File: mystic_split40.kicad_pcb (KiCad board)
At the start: 2 copper layers, 95.2 x 93.8 mm, 121 parts, among them J15 RESET, J16 ISP, J17 WS2812, J18 SJ-43514-SMT, J22 AREF, J25 TYPE-C-31-M-12, J33 RESET, J34 ISP, J35 WS2812, J36 SJ-43514-SMT, J4 AREF, J7 TYPE-C-31-M-12, SW1 EC11E, SW2 EC11E, U1 ATmega32U4-AU, U2 ATmega32U4-AU, Y1 CSTNE16M0VH3L000R0, Y2 CSTNE16M0VH3L000R0

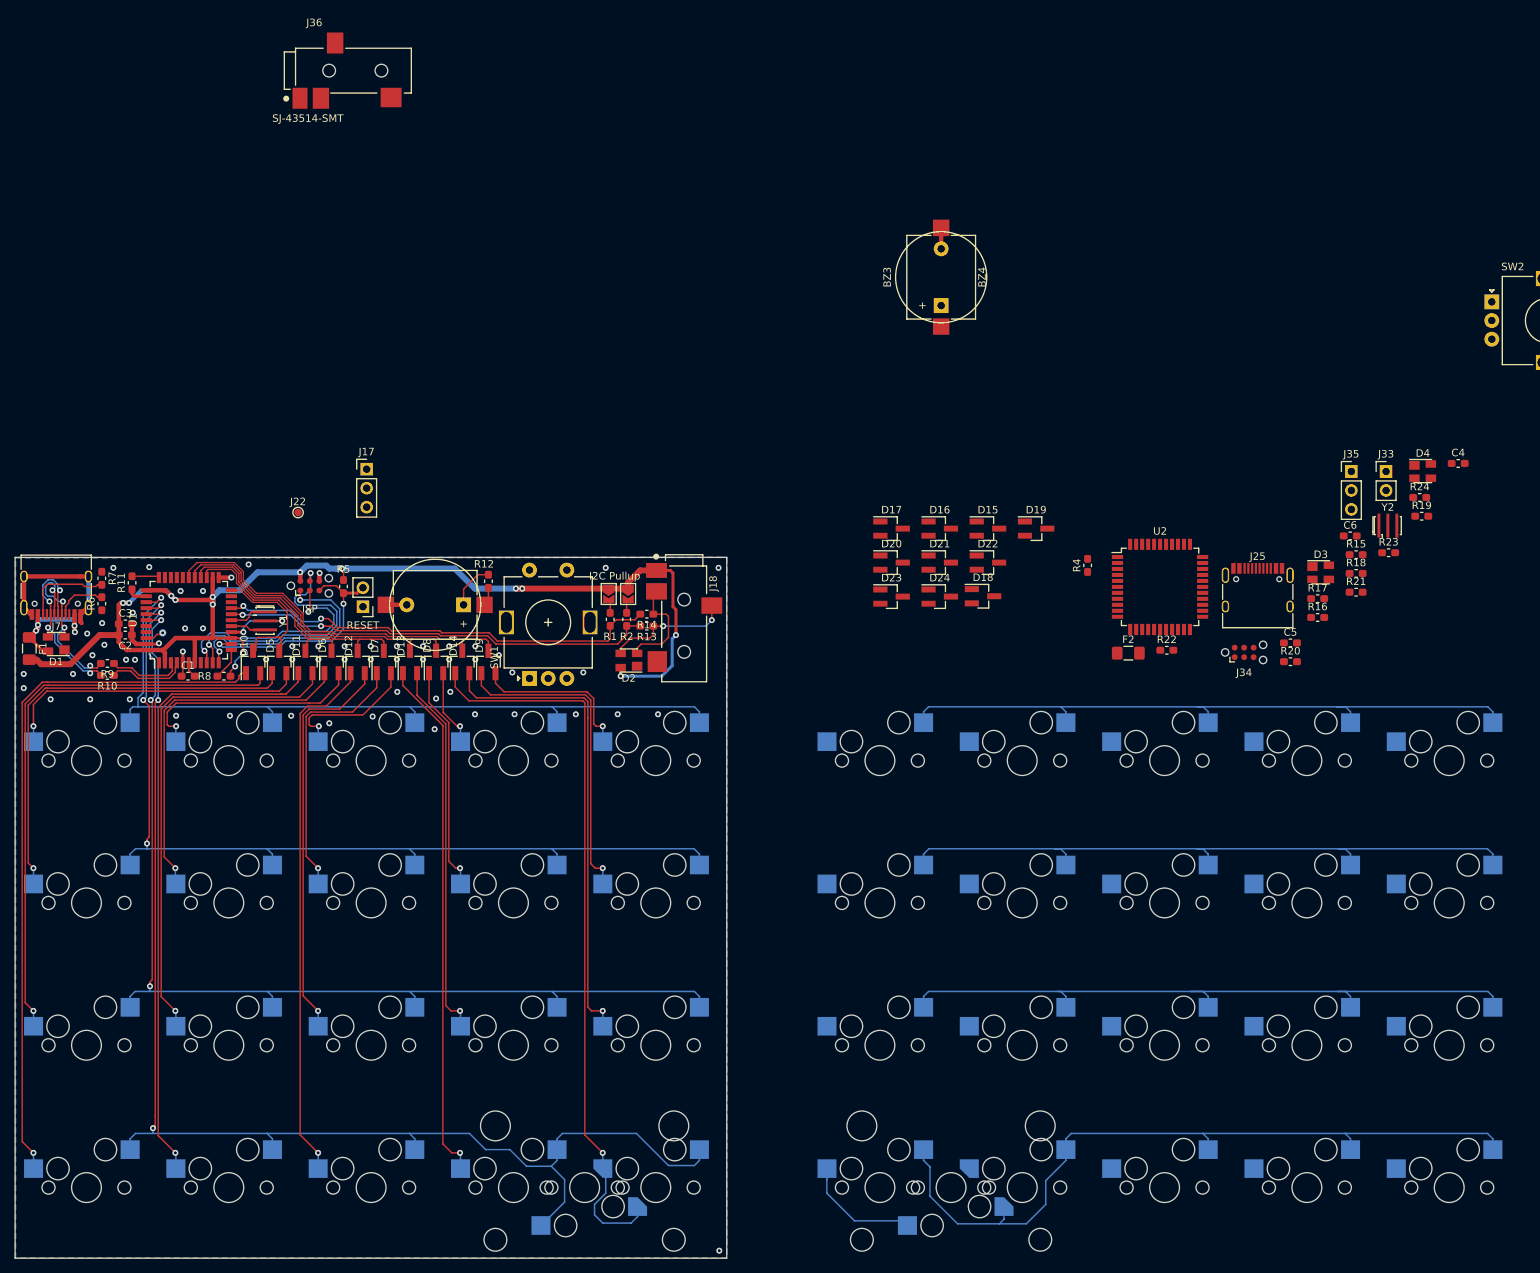
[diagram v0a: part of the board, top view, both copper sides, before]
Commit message: Added 3D models, prettied up silk
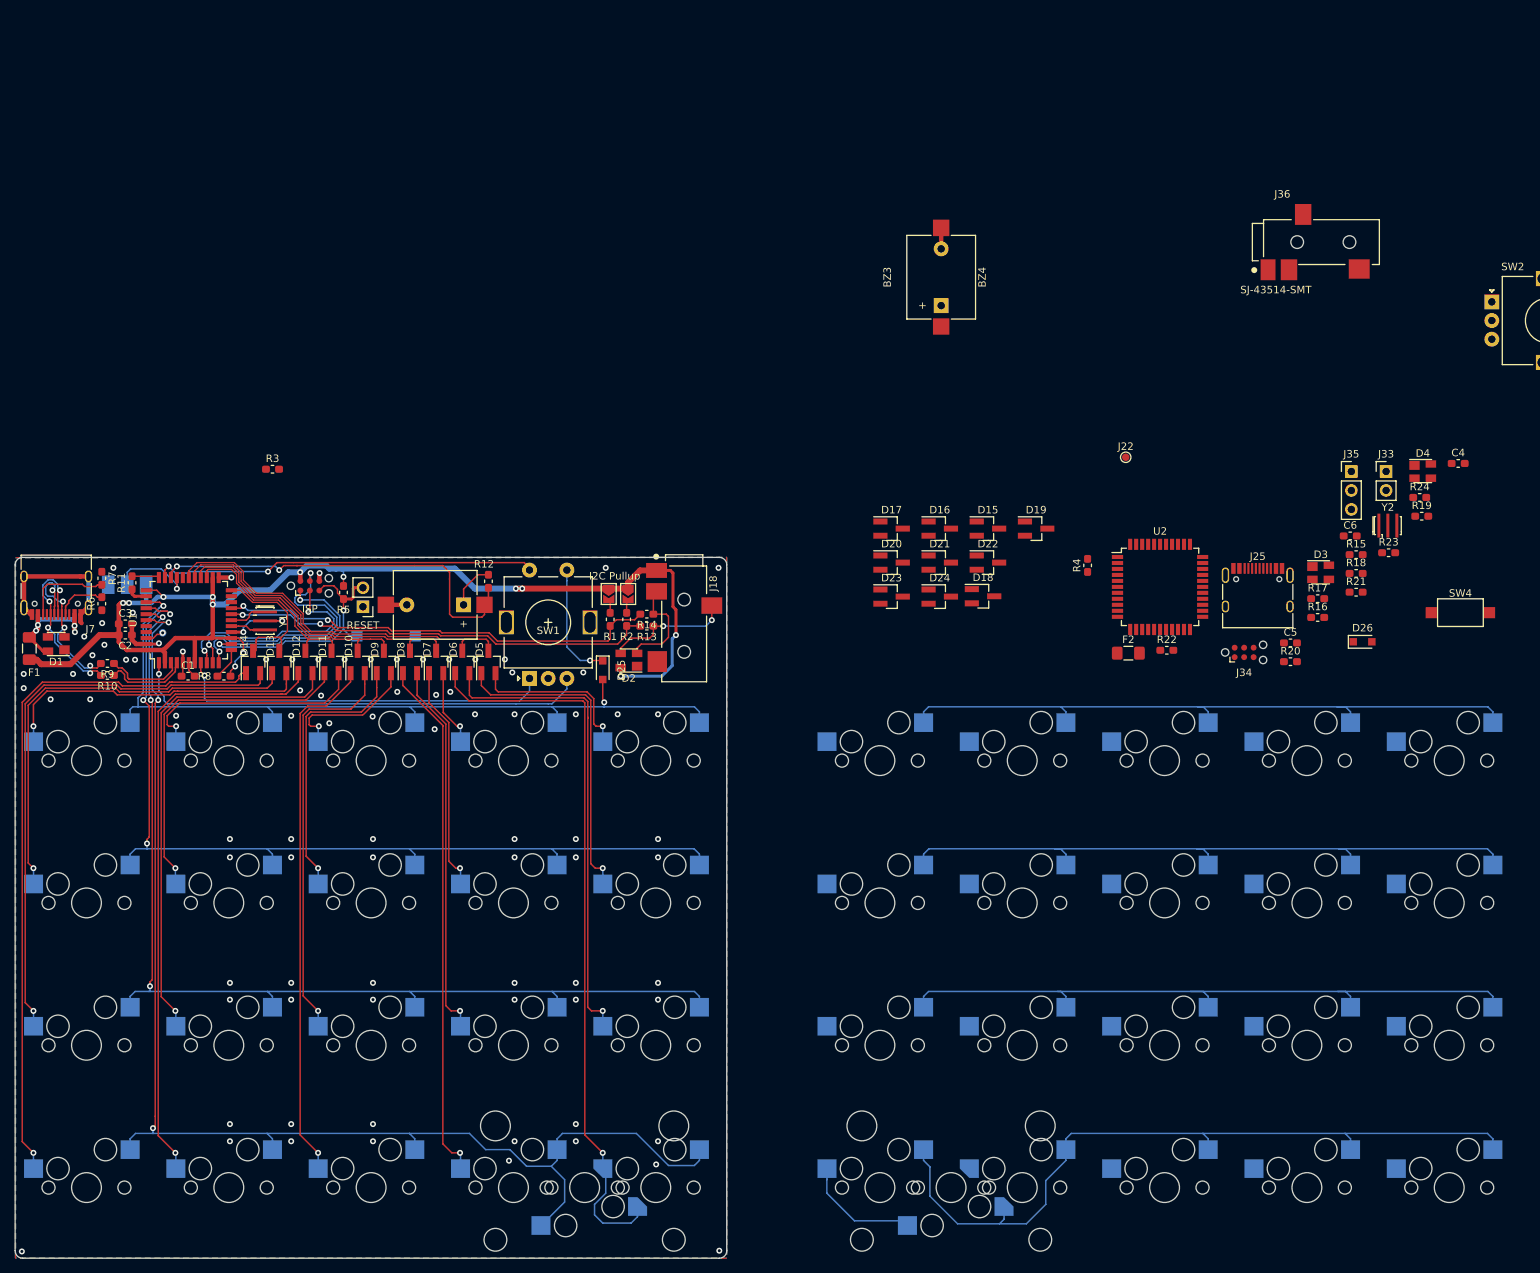
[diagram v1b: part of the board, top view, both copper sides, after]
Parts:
- added D25: BAV70, Diode_SMD:D_SOD-323_HandSoldering, F.Cu at (118.9, 27.8)
- added D26: BAV70, Diode_SMD:D_SOD-323_HandSoldering, F.Cu at (220.6, 24.0)
- added R3: 220R, Resistor_SMD:R_0603_1608Metric_Pad1.05x0.95mm_HandSolder, F.Cu at (74.7, 0.90)
- added SW3: Reset, Button_Switch_SMD:SW_SPST_CK_RS282G05A3, B.Cu at (89.9, 23.2)
- added SW4: Reset, Button_Switch_SMD:SW_SPST_CK_RS282G05A3, F.Cu at (233.7, 20.1)
- J17: moved to B.Cu
- R4: value 5k1 -> 220R
- moved J36 131.6 mm to (215.1, -29.5)
- moved J22 111.0 mm to (188.9, -0.70)
- moved J17 37.9 mm to (52.7, 16.4), turned to 270 degrees
- moved R5 0.80 mm to (84.2, 17.4)
- renumbered D12 to D10, D6 to D11, D11 to D12, D5 to D13, D10 to D14, D9 to D5, D14 to D6, D8 to D7, D13 to D8, D7 to D9
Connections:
- D15 pad 3: /Matrix right/col0 -> /Matrix right/col4
- D16 pad 3: /Matrix right/col1 -> /Matrix right/col4
- D17 pad 3: /Matrix right/col2 -> /Matrix right/col3
- D19 pad 3: /Matrix right/col4 -> /Matrix right/col2
- D20 pad 3: /Matrix right/col0 -> /Matrix right/col2
- D22 pad 3: /Matrix right/col2 -> /Matrix right/col1
- D23 pad 3: /Matrix right/col3 -> /Matrix right/col0
- D24 pad 3: /Matrix right/col4 -> /Matrix right/col0
- J25 pad A8: Net-(J25-PadA8) -> (no net)
- J25 pad B8: Net-(J25-PadB8) -> (no net)
- J7 pad A8: Net-(J7-PadA8) -> (no net)
- J7 pad B8: Net-(J7-PadB8) -> (no net)
- MX21 pad 1: Net-(D15-Pad2) -> Net-(D23-Pad2)
- MX22 pad 1: Net-(D16-Pad2) -> Net-(D21-Pad2)
- MX23 pad 1: Net-(D17-Pad2) -> Net-(D19-Pad2)
- MX24 pad 1: Net-(D18-Pad2) -> Net-(D17-Pad2)
- MX25 pad 1: Net-(D19-Pad2) -> Net-(D15-Pad2)
- MX26 pad 1: Net-(D15-Pad1) -> Net-(D23-Pad1)
- MX27 pad 1: Net-(D16-Pad1) -> Net-(D21-Pad1)
- MX28 pad 1: Net-(D17-Pad1) -> Net-(D19-Pad1)
- MX29 pad 1: Net-(D18-Pad1) -> Net-(D17-Pad1)
- MX30 pad 1: Net-(D19-Pad1) -> Net-(D15-Pad1)
- MX31 pad 1: Net-(D20-Pad2) -> Net-(D24-Pad2)
- MX32 pad 1: Net-(D21-Pad2) -> Net-(D22-Pad2)
- MX33 pad 1: Net-(D22-Pad2) -> Net-(D20-Pad2)
- MX34 pad 1: Net-(D23-Pad2) -> Net-(D18-Pad2)
- MX35 pad 1: Net-(D24-Pad2) -> Net-(D16-Pad2)
- MX36 pad 1: Net-(D20-Pad1) -> Net-(D24-Pad1)
- MX37 pad 1: Net-(D21-Pad1) -> Net-(D22-Pad1)
- MX38 pad 1: Net-(D22-Pad1) -> Net-(D20-Pad1)
- MX39 pad 1: Net-(D23-Pad1) -> Net-(D18-Pad1)
- MX40 pad 1: Net-(D24-Pad1) -> Net-(D16-Pad1)
- MX42 pad 1: Net-(D24-Pad1) -> Net-(D16-Pad1)
- R4 pad 1: GND -> (no net)
- SW1 pad MP: GND -> (no net)
- SW1 pad S1: /Left MCU/Enc_SW -> Net-(D25-Pad1)
- SW1 pad S2: GND -> /Left MCU/Enc_S1
- SW2 pad S1: /Right MCU/Enc_SW -> Net-(D26-Pad1)
- SW2 pad S2: GND -> /Right MCU/Enc_S1
- U1 pad 1: Net-(U1-Pad1) -> /Left MCU/Enc_B
- U1 pad 20: Net-(U1-Pad20) -> (no net)
- U1 pad 21: Net-(U1-Pad21) -> (no net)
- U1 pad 29: Net-(U1-Pad29) -> (no net)
- U1 pad 30: Net-(U1-Pad30) -> /Left MCU/WS2812_out
- U1 pad 31: Net-(U1-Pad31) -> /Left MCU/buzz
- U1 pad 32: Net-(U1-Pad32) -> /Left MCU/Enc_S1
- U1 pad 40: Net-(U1-Pad40) -> (no net)
- U1 pad 41: Net-(U1-Pad41) -> (no net)
- U1 pad 8: Net-(U1-Pad8) -> /Left MCU/Enc_A
- U2 pad 1: Net-(U2-Pad1) -> /Right MCU/Enc_B
- U2 pad 20: Net-(U2-Pad20) -> (no net)
- U2 pad 21: Net-(U2-Pad21) -> (no net)
- U2 pad 29: Net-(U2-Pad29) -> (no net)
- U2 pad 30: Net-(U2-Pad30) -> /Right MCU/WS2812_out
- U2 pad 31: Net-(U2-Pad31) -> /Right MCU/buzz
- U2 pad 32: Net-(U2-Pad32) -> /Right MCU/Enc_S1
- U2 pad 40: Net-(U2-Pad40) -> (no net)
- U2 pad 41: Net-(U2-Pad41) -> (no net)
- U2 pad 8: Net-(U2-Pad8) -> /Right MCU/Enc_A
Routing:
- net /Left MCU/Enc_B: track 0.00 -> 61.7 mm, vias 0 -> 1
- net /Left MCU/Enc_S1: track 0.00 -> 51.2 mm, vias 0 -> 2
- net /Left MCU/buzz: track 2.49 -> 53.6 mm, vias 0 -> 2
- net /Left MCU/Enc_A: track 0.00 -> 50.9 mm, vias 0 -> 1
- net Net-(D25-Pad1): track 0.00 -> 15.9 mm, vias 0 -> 1
- net Net-(D24-Pad1): track 15.0 -> 0.00 mm
- net Net-(D16-Pad1): track 0.00 -> 15.0 mm
- net /Left MCU/WS2812_out: track 0.00 -> 11.4 mm, vias 0 -> 1
- net /Left MCU/row0: track 105.2 -> 108.4 mm, vias 1 -> 2
- net /Left MCU/~reset: track 31.0 -> 34.1 mm
- net /Left MCU/row1: track 123.3 -> 125.3 mm
- net /Left MCU/row3: track 173.6 -> 175.2 mm
- net Net-(D10-Pad2): track 53.9 -> 54.8 mm
- net /Left MCU/D-: track 9.79 -> 10.6 mm
- net +5V: track 166.9 -> 167.8 mm, vias 14 -> 13
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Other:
- outline, holes or cut-outs redrawn

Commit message: Copied left half layout to right components
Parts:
- removed the BZ3 at (164.2, -21.0)
- removed the BZ4 at (164.2, -24.8)
- removed the C4 at (233.4, 0.13)
- removed the C5 at (210.9, 24.1)
- removed the C6 at (218.9, 9.83)
- removed the D15 at (170.5, 8.85)
- removed the D16 at (164.0, 8.85)
- removed the D17 at (157.6, 8.85)
- removed the D18 at (169.8, 17.9)
- removed the D19 at (176.9, 8.85)
- removed the D20 at (157.6, 13.4)
- removed the D21 at (164.0, 13.4)
- removed the D22 at (170.5, 13.4)
- removed the D23 at (157.6, 17.9)
- removed the D24 at (164.0, 17.9)
- removed the D26 at (220.6, 24.0)
- removed the D3 at (215.0, 14.7)
- removed the D4 at (228.7, 1.15)
- removed the F2 at (189.2, 25.5)
- removed the J25 at (206.6, 18.2)
- removed the J33 at (223.8, 1.20)
- removed the J34 at (204.8, 25.4)
- removed the J36 at (215.1, -29.5)
- removed the MX21 at (232.2, 39.9)
- removed the MX22 at (213.2, 39.9)
- removed the MX23 at (194.1, 39.9)
- removed the MX24 at (175.1, 39.9)
- removed the MX26 at (232.2, 59.0)
- removed the MX27 at (213.2, 59.0)
- removed the MX28 at (194.1, 59.0)
- removed the MX29 at (175.1, 59.0)
- removed the MX31 at (232.2, 78.0)
- removed the MX32 at (213.2, 78.0)
- removed the MX33 at (194.1, 78.0)
- removed the MX34 at (175.1, 78.0)
- removed the MX36 at (232.2, 97.0)
- removed the MX37 at (213.2, 97.0)
- removed the MX38 at (194.1, 97.0)
- removed the MX39 at (175.1, 97.0)
- removed the R16 at (214.6, 20.7)
- removed the R17 at (214.6, 18.2)
- removed the R18 at (219.7, 14.8)
- removed the R19 at (228.5, 7.19)
- removed the R20 at (210.9, 26.7)
- removed the R21 at (219.7, 17.4)
- removed the R22 at (194.4, 25.1)
- removed the R23 at (224.1, 12.1)
- removed the R24 at (228.2, 4.68)
- removed the R4 at (183.8, 13.8)
- removed the SW2 at (237.9, -21.5)
- removed the SW4 at (233.7, 20.1)
- removed the U2 at (193.5, 16.6)
- removed the Y2 at (224.0, 8.45)
- added BZ3: Buzzer_magnetic, Buzzer_Beeper:Buzzer_12x9.5RM7.6, F.Cu at (225.5, 19.1)
- added BZ3: Buzzer_magnetic, Buzzer_Beeper:Buzzer_12x9.5RM7.6, F.Cu at (-156.3, 100.3)
- added BZ4: Buzzer_piezo, Buzzer_Beeper:Buzzer_Mallory_AST1109MLTRQ, F.Cu at (221.7, 19.1)
- added BZ4: Buzzer_piezo, Buzzer_Beeper:Buzzer_Mallory_AST1109MLTRQ, F.Cu at (-156.3, 96.5)
- added C4: 1uF, Capacitor_SMD:C_0603_1608Metric_Pad1.05x0.95mm_HandSolder, F.Cu at (188.7, 28.6)
- added C4: 1uF, Capacitor_SMD:C_0603_1608Metric_Pad1.05x0.95mm_HandSolder, F.Cu at (-87.2, 121.5)
- added C5: 100nF, Capacitor_SMD:C_0603_1608Metric_Pad1.05x0.95mm_HandSolder, F.Cu at (180.2, 23.1)
- added C5: 100nF, Capacitor_SMD:C_0603_1608Metric_Pad1.05x0.95mm_HandSolder, F.Cu at (-109.6, 145.5)
- added C6: 1uF, Capacitor_SMD:C_0603_1608Metric_Pad1.05x0.95mm_HandSolder, F.Cu at (180.2, 21.6)
- added C6: 1uF, Capacitor_SMD:C_0603_1608Metric_Pad1.05x0.95mm_HandSolder, F.Cu at (-101.6, 131.2)
- added D15: BAV70, Package_TO_SOT_SMD:SOT-23_Handsoldering, F.Cu at (228.8, 26.7)
- added D15: BAV70, Package_TO_SOT_SMD:SOT-23_Handsoldering, F.Cu at (-150.1, 130.2)
- added D16: BAV70, Package_TO_SOT_SMD:SOT-23_Handsoldering, F.Cu at (225.3, 26.7)
- added D16: BAV70, Package_TO_SOT_SMD:SOT-23_Handsoldering, F.Cu at (-156.5, 130.2)
- added D17: BAV70, Package_TO_SOT_SMD:SOT-23_Handsoldering, F.Cu at (221.8, 26.7)
- added D17: BAV70, Package_TO_SOT_SMD:SOT-23_Handsoldering, F.Cu at (-163.0, 130.2)
- added D18: BAV70, Package_TO_SOT_SMD:SOT-23_Handsoldering, F.Cu at (218.3, 26.7)
- added D18: BAV70, Package_TO_SOT_SMD:SOT-23_Handsoldering, F.Cu at (-150.8, 139.2)
- added D19: BAV70, Package_TO_SOT_SMD:SOT-23_Handsoldering, F.Cu at (214.8, 26.7)
- added D19: BAV70, Package_TO_SOT_SMD:SOT-23_Handsoldering, F.Cu at (-143.6, 130.2)
- added D20: BAV70, Package_TO_SOT_SMD:SOT-23_Handsoldering, F.Cu at (211.3, 26.7)
- added D20: BAV70, Package_TO_SOT_SMD:SOT-23_Handsoldering, F.Cu at (-163.0, 134.8)
- added D21: BAV70, Package_TO_SOT_SMD:SOT-23_Handsoldering, F.Cu at (207.8, 26.7)
- added D21: BAV70, Package_TO_SOT_SMD:SOT-23_Handsoldering, F.Cu at (-156.5, 134.8)
- added D22: BAV70, Package_TO_SOT_SMD:SOT-23_Handsoldering, F.Cu at (204.3, 26.7)
- added D22: BAV70, Package_TO_SOT_SMD:SOT-23_Handsoldering, F.Cu at (-150.1, 134.8)
- added D23: BAV70, Package_TO_SOT_SMD:SOT-23_Handsoldering, F.Cu at (200.8, 26.7)
- added D23: BAV70, Package_TO_SOT_SMD:SOT-23_Handsoldering, F.Cu at (-163.0, 139.3)
- added D24: BAV70, Package_TO_SOT_SMD:SOT-23_Handsoldering, F.Cu at (197.3, 26.7)
- added D24: BAV70, Package_TO_SOT_SMD:SOT-23_Handsoldering, F.Cu at (-156.5, 139.3)
- added D26: BAV70, Diode_SMD:D_SOD-323_HandSoldering, F.Cu at (242.9, 29.2)
- added D26: BAV70, Diode_SMD:D_SOD-323_HandSoldering, F.Cu at (-100.0, 145.3)
- added D27: Red LED, LED_SMD:LED_0805_2012Metric_Pad1.15x1.40mm_HandSolder, B.Cu at (96.8, 22.1)
- added D28: Red LED, LED_SMD:LED_0805_2012Metric_Pad1.15x1.40mm_HandSolder, B.Cu at (222.1, 22.1)
- added D28: Red LED, LED_SMD:LED_0805_2012Metric_Pad1.15x1.40mm_HandSolder, F.Cu at (-126.0, 121.8)
- added D3: PRTR5V0U2X, Package_TO_SOT_SMD:SOT-143, F.Cu at (173.2, 24.3)
- added D3: PRTR5V0U2X, Package_TO_SOT_SMD:SOT-143, F.Cu at (-105.6, 136.1)
- added D4: PRTR5V0U2X, Package_TO_SOT_SMD:SOT-143, F.Cu at (246.4, 26.2)
- added D4: PRTR5V0U2X, Package_TO_SOT_SMD:SOT-143, F.Cu at (-91.9, 122.5)
- added F2: ?mA fuse, Fuse:Fuse_1206_3216Metric_Pad1.42x1.75mm_HandSolder, F.Cu at (169.6, 24.9)
- added F2: ?mA fuse, Fuse:Fuse_1206_3216Metric_Pad1.42x1.75mm_HandSolder, F.Cu at (-131.3, 146.9)
- added G***: LOGO, graphics:kiwi10mm, B.Cu at (250.6, 32.9)
- added G***: LOGO, graphics:kiwi10mm, B.Cu at (125.3, 32.9)
- added J25: TYPE-C-31-M-12, Connector_USB:USB_C_Receptacle_HRO_TYPE-C-31-M-12, F.Cu at (173.2, 16.3)
- added J25: TYPE-C-31-M-12, Connector_USB:USB_C_Receptacle_HRO_TYPE-C-31-M-12, F.Cu at (-114.0, 139.6)
- added J33: RESET, Connector_PinHeader_2.54mm:PinHeader_1x02_P2.54mm_Vertical, F.Cu at (212.1, 19.3)
- added J33: RESET, Connector_PinHeader_2.54mm:PinHeader_1x02_P2.54mm_Vertical, F.Cu at (-96.8, 122.5)
- added J34: ISP, Connector:Tag-Connect_TC2030-IDC-NL_2x03_P1.27mm_Vertical, F.Cu at (204.9, 16.5)
- added J34: ISP, Connector:Tag-Connect_TC2030-IDC-NL_2x03_P1.27mm_Vertical, F.Cu at (-115.8, 146.8)
- added J36: SJ-43514-SMT, CUI:SJ-43514-SMT, F.Cu at (254.2, 21.6)
- added J36: SJ-43514-SMT, CUI:SJ-43514-SMT, F.Cu at (-105.5, 91.8)
- added J4: AREF, TestPoint:TestPoint_Pad_D1.0mm, B.Cu at (185.2, 22.8)
- added MX21: MX-NoLED, Ai03-MX:MXOnly-1U-Hotswap, F.Cu at (175.1, 44.9)
- added MX21: MX-NoLED, Ai03-MX:MXOnly-1U-Hotswap, F.Cu at (-88.3, 161.2)
- added MX22: MX-NoLED, Ai03-MX:MXOnly-1U-Hotswap, F.Cu at (194.1, 44.9)
- added MX22: MX-NoLED, Ai03-MX:MXOnly-1U-Hotswap, F.Cu at (-107.4, 161.2)
- added MX23: MX-NoLED, Ai03-MX:MXOnly-1U-Hotswap, F.Cu at (213.2, 44.9)
- added MX23: MX-NoLED, Ai03-MX:MXOnly-1U-Hotswap, F.Cu at (-126.5, 161.2)
- added MX24: MX-NoLED, Ai03-MX:MXOnly-1U-Hotswap, F.Cu at (232.2, 44.9)
- added MX24: MX-NoLED, Ai03-MX:MXOnly-1U-Hotswap, F.Cu at (-145.5, 161.2)
- added MX25: MX-NoLED, Ai03-MX:MXOnly-1U-Hotswap, F.Cu at (251.2, 44.9)
- added MX26: MX-NoLED, Ai03-MX:MXOnly-1U-Hotswap, F.Cu at (175.1, 64.0)
- added MX26: MX-NoLED, Ai03-MX:MXOnly-1U-Hotswap, F.Cu at (-88.3, 180.3)
- added MX27: MX-NoLED, Ai03-MX:MXOnly-1U-Hotswap, F.Cu at (194.1, 64.0)
- added MX27: MX-NoLED, Ai03-MX:MXOnly-1U-Hotswap, F.Cu at (-107.4, 180.3)
- added MX28: MX-NoLED, Ai03-MX:MXOnly-1U-Hotswap, F.Cu at (213.2, 64.0)
- added MX28: MX-NoLED, Ai03-MX:MXOnly-1U-Hotswap, F.Cu at (-126.5, 180.3)
- added MX29: MX-NoLED, Ai03-MX:MXOnly-1U-Hotswap, F.Cu at (232.2, 64.0)
- added MX29: MX-NoLED, Ai03-MX:MXOnly-1U-Hotswap, F.Cu at (-145.5, 180.3)
- added MX30: MX-NoLED, Ai03-MX:MXOnly-1U-Hotswap, F.Cu at (251.2, 64.0)
- added MX31: MX-NoLED, Ai03-MX:MXOnly-1U-Hotswap, F.Cu at (175.1, 83.0)
- added MX31: MX-NoLED, Ai03-MX:MXOnly-1U-Hotswap, F.Cu at (-88.3, 199.3)
- added MX32: MX-NoLED, Ai03-MX:MXOnly-1U-Hotswap, F.Cu at (194.1, 83.0)
- added MX32: MX-NoLED, Ai03-MX:MXOnly-1U-Hotswap, F.Cu at (-107.4, 199.3)
- added MX33: MX-NoLED, Ai03-MX:MXOnly-1U-Hotswap, F.Cu at (213.2, 83.0)
- added MX33: MX-NoLED, Ai03-MX:MXOnly-1U-Hotswap, F.Cu at (-126.5, 199.3)
- added MX34: MX-NoLED, Ai03-MX:MXOnly-1U-Hotswap, F.Cu at (232.2, 83.0)
- added MX34: MX-NoLED, Ai03-MX:MXOnly-1U-Hotswap, F.Cu at (-145.5, 199.3)
- added MX35: MX-NoLED, Ai03-MX:MXOnly-1U-Hotswap, F.Cu at (251.2, 83.0)
- added MX36: MX-NoLED, Ai03-MX:MXOnly-1U-Hotswap, F.Cu at (175.1, 102.0)
- added MX36: MX-NoLED, Ai03-MX:MXOnly-1U-Hotswap, F.Cu at (-88.3, 218.4)
- added MX37: MX-NoLED, Ai03-MX:MXOnly-1U-Hotswap, F.Cu at (194.1, 102.0)
- added MX37: MX-NoLED, Ai03-MX:MXOnly-1U-Hotswap, F.Cu at (-107.4, 218.4)
- added MX38: MX-NoLED, Ai03-MX:MXOnly-1U-Hotswap, F.Cu at (213.2, 102.0)
- added MX38: MX-NoLED, Ai03-MX:MXOnly-1U-Hotswap, F.Cu at (-126.5, 218.4)
- added MX39: MX-NoLED, Ai03-MX:MXOnly-1U-Hotswap, F.Cu at (232.2, 102.0)
- added MX39: MX-NoLED, Ai03-MX:MXOnly-1U-Hotswap, F.Cu at (-145.5, 218.4)
- added MX40: MX-NoLED, Ai03-MX:MXOnly-1U-Hotswap, F.Cu at (251.2, 102.0)
- added MX42: MX-NoLED, Ai03-MX:MXOnly-2U-Hotswap, F.Cu at (241.7, 102.0)
- added R16: 5k1, Resistor_SMD:R_0603_1608Metric_Pad1.05x0.95mm_HandSolder, F.Cu at (179.3, 18.9)
- added R16: 5k1, Resistor_SMD:R_0603_1608Metric_Pad1.05x0.95mm_HandSolder, F.Cu at (-106.0, 142.1)
- added R17: 5k1, Resistor_SMD:R_0603_1608Metric_Pad1.05x0.95mm_HandSolder, F.Cu at (179.3, 15.5)
- added R17: 5k1, Resistor_SMD:R_0603_1608Metric_Pad1.05x0.95mm_HandSolder, F.Cu at (-106.0, 139.6)
- added R18: 220R, Resistor_SMD:R_0603_1608Metric_Pad1.05x0.95mm_HandSolder, F.Cu at (193.4, 28.6)
- added R18: 220R, Resistor_SMD:R_0603_1608Metric_Pad1.05x0.95mm_HandSolder, F.Cu at (-100.8, 136.2)
- added R19: 22R, Resistor_SMD:R_0603_1608Metric_Pad1.05x0.95mm_HandSolder, F.Cu at (180.1, 26.9)
- added R19: 22R, Resistor_SMD:R_0603_1608Metric_Pad1.05x0.95mm_HandSolder, F.Cu at (-92.0, 128.5)
- added R20: 22R, Resistor_SMD:R_0603_1608Metric_Pad1.05x0.95mm_HandSolder, F.Cu at (180.1, 28.5)
- added R20: 22R, Resistor_SMD:R_0603_1608Metric_Pad1.05x0.95mm_HandSolder, F.Cu at (-109.6, 148.0)
- added R21: 5k1, Resistor_SMD:R_0603_1608Metric_Pad1.05x0.95mm_HandSolder, F.Cu at (181.2, 16.1)
- added R21: 5k1, Resistor_SMD:R_0603_1608Metric_Pad1.05x0.95mm_HandSolder, F.Cu at (-100.8, 138.7)
- added R22: 220R, Resistor_SMD:R_0603_1608Metric_Pad1.05x0.95mm_HandSolder, F.Cu at (228.8, 15.9)
- added R22: 220R, Resistor_SMD:R_0603_1608Metric_Pad1.05x0.95mm_HandSolder, F.Cu at (-126.2, 146.5)
- added R23: 220R, Resistor_SMD:R_0603_1608Metric_Pad1.05x0.95mm_HandSolder, F.Cu at (248.9, 21.0)
- added R23: 220R, Resistor_SMD:R_0603_1608Metric_Pad1.05x0.95mm_HandSolder, F.Cu at (-96.5, 133.4)
- added R24: 220R, Resistor_SMD:R_0603_1608Metric_Pad1.05x0.95mm_HandSolder, F.Cu at (246.1, 23.6)
- added R24: 220R, Resistor_SMD:R_0603_1608Metric_Pad1.05x0.95mm_HandSolder, F.Cu at (-92.3, 126.0)
- added R4: 220R, Resistor_SMD:R_0603_1608Metric_Pad1.05x0.95mm_HandSolder, B.Cu at (222.1, 20.3)
- added R4: 220R, Resistor_SMD:R_0603_1608Metric_Pad1.05x0.95mm_HandSolder, F.Cu at (-136.8, 135.1)
- added R5: 5k1, Resistor_SMD:R_0603_1608Metric_Pad1.05x0.95mm_HandSolder, F.Cu at (209.4, 17.4)
- added REF**: MountingHole_2.2mm_M2_DIN965, MountingHole:MountingHole_2.2mm_M2_DIN965, F.Cu at (167.0, 31.7)
- added REF**: MountingHole_2.2mm_M2_DIN965, MountingHole:MountingHole_2.2mm_M2_DIN965, F.Cu at (134.0, 14.7)
- added REF**: MountingHole_3.2mm_M3_DIN965_Pad, MountingHole:MountingHole_3.2mm_M3_DIN965_Pad, F.Cu at (59.3, 54.4)
- added REF**: MountingHole_3.2mm_M3_DIN965_Pad, MountingHole:MountingHole_3.2mm_M3_DIN965_Pad, F.Cu at (116.5, 54.4)
- added REF**: MountingHole_3.2mm_M3_DIN965_Pad, MountingHole:MountingHole_3.2mm_M3_DIN965_Pad, F.Cu at (97.4, 92.5)
- added REF**: MountingHole_3.2mm_M3_DIN965_Pad, MountingHole:MountingHole_3.2mm_M3_DIN965_Pad, F.Cu at (78.3, 92.5)
- added REF**: MountingHole_2.2mm_M2_DIN965, MountingHole:MountingHole_2.2mm_M2_DIN965, F.Cu at (134.0, 31.7)
- added REF**: MountingHole_2.2mm_M2_DIN965, MountingHole:MountingHole_2.2mm_M2_DIN965, F.Cu at (41.8, 31.7)
- added REF**: MountingHole_2.2mm_M2_DIN965, MountingHole:MountingHole_2.2mm_M2_DIN965, F.Cu at (259.2, 31.7)
- added REF**: MountingHole_3.2mm_M3_DIN965_Pad, MountingHole:MountingHole_3.2mm_M3_DIN965_Pad, F.Cu at (222.7, 92.5)
- added REF**: MountingHole_3.2mm_M3_DIN965_Pad, MountingHole:MountingHole_3.2mm_M3_DIN965_Pad, F.Cu at (203.6, 92.5)
- added REF**: MountingHole_3.2mm_M3_DIN965_Pad, MountingHole:MountingHole_3.2mm_M3_DIN965_Pad, F.Cu at (241.7, 54.4)
- added REF**: MountingHole_3.2mm_M3_DIN965_Pad, MountingHole:MountingHole_3.2mm_M3_DIN965_Pad, F.Cu at (184.6, 54.4)
- added REF**: MountingHole_2.2mm_M2_DIN965, MountingHole:MountingHole_2.2mm_M2_DIN965, F.Cu at (259.2, 14.7)
- added REF**: MountingHole_2.2mm_M2_DIN965, MountingHole:MountingHole_2.2mm_M2_DIN965, F.Cu at (167.0, 14.7)
- added REF**: MountingHole_2.2mm_M2_DIN965, MountingHole:MountingHole_2.2mm_M2_DIN965, F.Cu at (41.8, 14.7)
- added SW2: EC11E, Rotary_Encoder:RotaryEncoder_Alps_EC11E-Switch_Vertical_H20mm, F.Cu at (234.3, 28.9)
- added SW2: EC11E, Rotary_Encoder:RotaryEncoder_Alps_EC11E-Switch_Vertical_H20mm, F.Cu at (-73.3, 103.0)
- added SW4: Reset, Button_Switch_SMD:SW_SPST_CK_RS282G05A3, B.Cu at (215.2, 23.2)
- added SW4: Reset, Button_Switch_SMD:SW_SPST_CK_RS282G05A3, F.Cu at (-86.8, 141.4)
- added U2: ATmega32U4-AU, Package_QFP:TQFP-44_10x10mm_P0.8mm, F.Cu at (188.8, 21.1)
- added U2: ATmega32U4-AU, Package_QFP:TQFP-44_10x10mm_P0.8mm, F.Cu at (-127.0, 138.0)
- added Y2: CSTNE16M0VH3L000R0, Crystal:Resonator_SMD_muRata_CSTxExxV-3Pin_3.0x1.1mm_HandSoldering, F.Cu at (198.9, 21.2)
- added Y2: CSTNE16M0VH3L000R0, Crystal:Resonator_SMD_muRata_CSTxExxV-3Pin_3.0x1.1mm_HandSoldering, F.Cu at (-96.6, 129.8)
- R3: moved to B.Cu
- moved J22 342.8 mm to (-131.7, 120.7)
- moved MX30 342.8 mm to (-164.6, 180.3)
- moved MX40 342.8 mm to (-164.6, 218.4)
- moved MX42 342.8 mm to (-155.0, 218.4)
- moved J35 342.8 mm to (-101.5, 122.5)
- moved MX25 342.8 mm to (-164.6, 161.2)
- moved MX35 342.8 mm to (-164.6, 199.3)
- moved R15 342.8 mm to (-100.8, 133.7)
- moved R3 29.4 mm to (96.8, 20.3), turned to 180 degrees
- moved R14 5.15 mm to (120.8, 23.6)
- moved MX1 5.00 mm to (49.8, 44.9)
- moved MX10 5.00 mm to (126.0, 64.0)
- moved MX11 5.00 mm to (49.8, 83.0)
- moved MX12 5.00 mm to (68.8, 83.0)
- moved MX13 5.00 mm to (87.9, 83.0)
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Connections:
- D2 pad 2: /Left MCU/Rr_1 -> /Left MCU/Rr_2
- D2 pad 3: /Left MCU/Rr_2 -> /Left MCU/Rr_1
- R3 pad 1: (no net) -> Net-(D27-Pad2)
- R3 pad 2: (no net) -> /Left MCU/DFU_LED
- U1 pad 29: (no net) -> /Left MCU/DFU_LED
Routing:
- net /Left MCU/row3: track 175.2 -> 359.6 mm, vias 3 -> 6
- net /Left MCU/row2: track 140.3 -> 296.2 mm, vias 3 -> 6
- net /Left MCU/row1: track 125.3 -> 266.7 mm, vias 3 -> 6
- net +5V: track 167.8 -> 296.5 mm, vias 13 -> 23
- net /Left MCU/row0: track 108.4 -> 236.5 mm, vias 2 -> 4
- net Net-(D6-Pad1): track 97.2 -> 210.0 mm, vias 1 -> 2
- net Net-(D14-Pad1): track 95.3 -> 197.9 mm, vias 1 -> 2
- net Net-(D12-Pad1): track 83.8 -> 183.1 mm, vias 1 -> 2
- net Net-(D14-Pad2): track 78.0 -> 163.5 mm, vias 1 -> 2
- net /Left MCU/DFU_LED: track 0.00 -> 85.3 mm, vias 0 -> 6
- net Net-(D10-Pad1): track 71.6 -> 154.8 mm, vias 1 -> 2
- net Net-(D12-Pad2): track 66.5 -> 148.4 mm, vias 1 -> 2
- net /Left MCU/Enc_B: track 61.7 -> 143.4 mm, vias 1 -> 2
- net Net-(D8-Pad1): track 70.2 -> 150.7 mm, vias 1 -> 2
- net Net-(D6-Pad2): track 64.4 -> 143.8 mm, vias 1 -> 2
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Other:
- board size 95.2 x 93.8 mm -> 220.5 x 98.8 mm
- board text added: "MS40"
- board text added: "V1.0"
- board text added: "git.io/MS40"
